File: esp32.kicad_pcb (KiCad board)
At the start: 2 copper layers, 44 x 80 mm, 102 parts, among them J1 USB_C, J14 PWR_CONN, J15 SPI_0, J16 SPI_1, J3 A0, J4 A1, J5 A2, J6 D0, J7 D1, J8 USB_VOUT, Q10 AO3400A, Q11 AO3400A, Q12 AO3400A, Q3 AO3400A, Q4 AO3400A, Q5 AO3400A, Q6 AO3400A, Q7 AO3400A, Q8 AO3400A, Q9 AO3400A, SW1 SW_RST, SW2 SW_BOOT, U1 LMR36520ADDAR, U3 ESP32-S3-WROOM-1

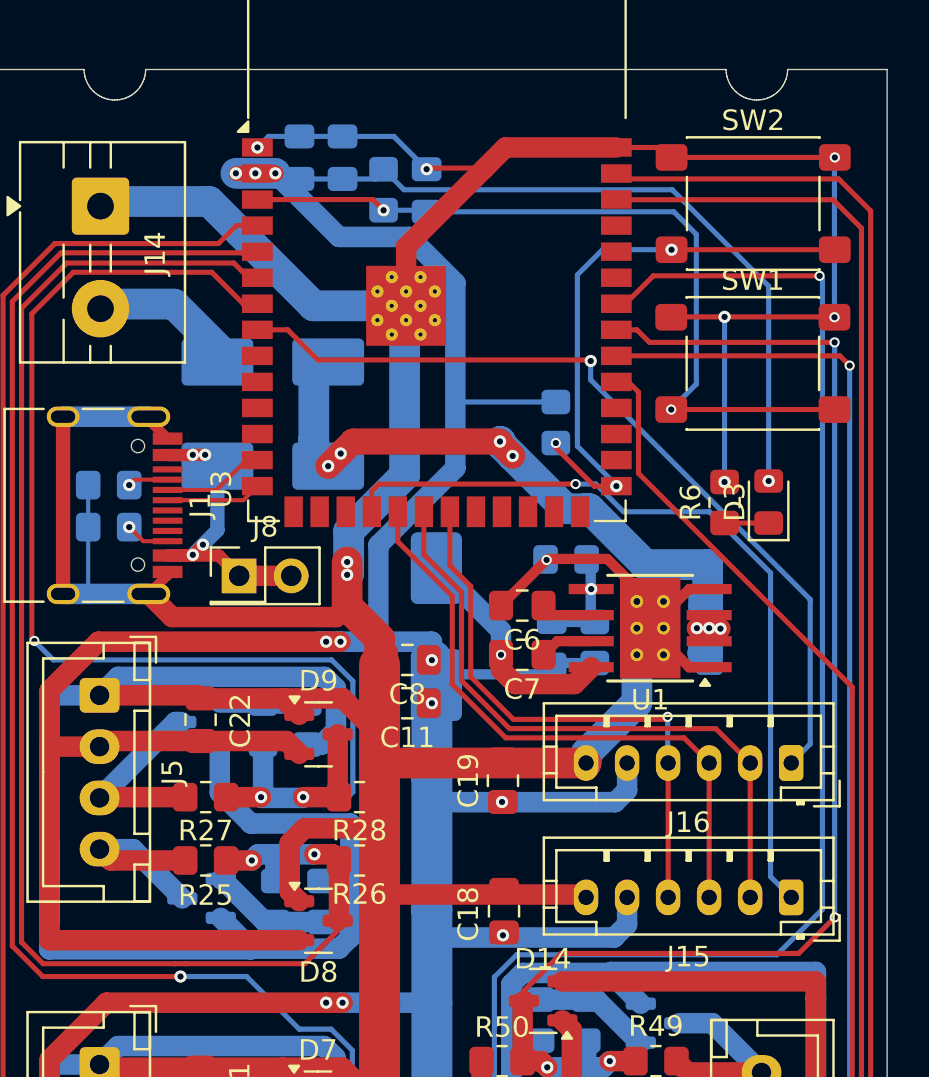
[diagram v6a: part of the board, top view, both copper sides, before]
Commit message: remove vias from pads
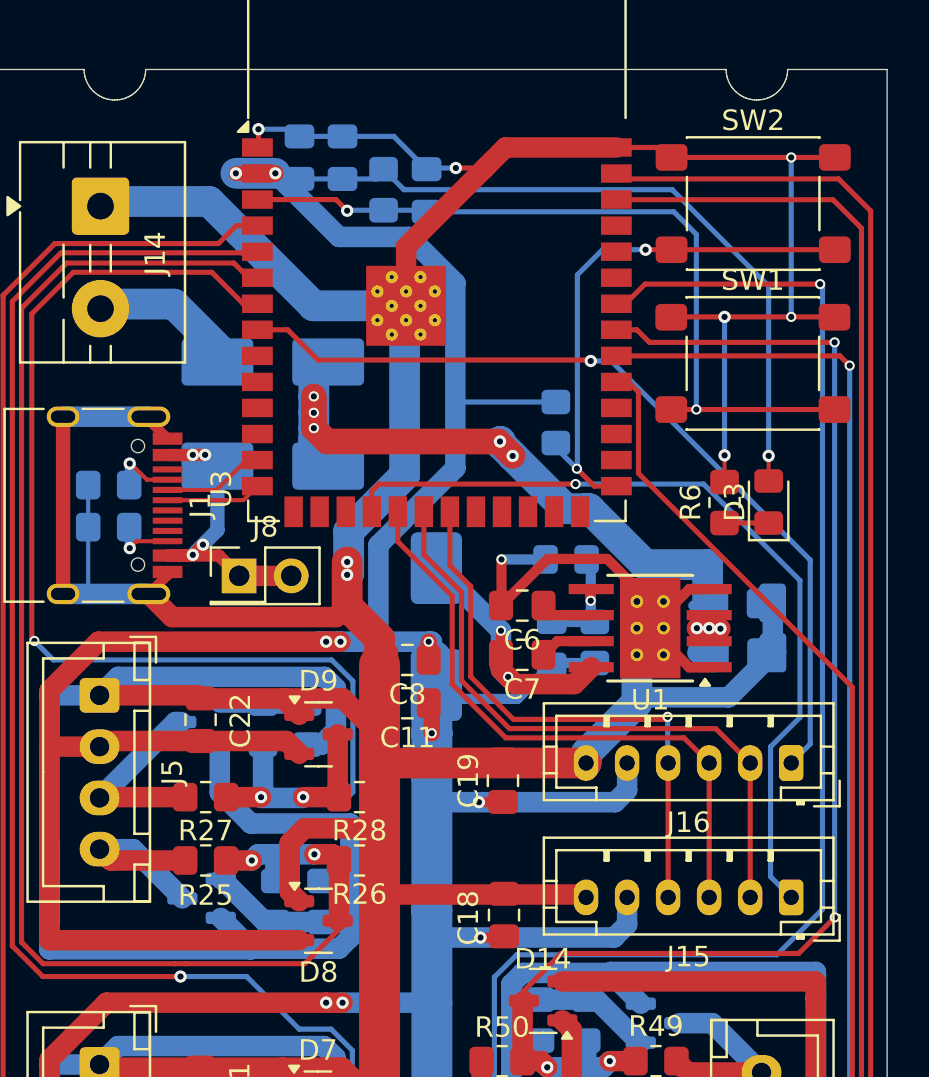
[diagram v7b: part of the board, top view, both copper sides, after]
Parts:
- moved C5 2.96 mm to (107.6, 99.4), turned to 0 degrees
- moved C4 2.93 mm to (107.6, 97.0), turned to 0 degrees
- moved C18 0.19 mm to (96.2, 112.2)
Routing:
- net GND: track 699.2 -> 714.5 mm
- net VCC: track 43.9 -> 38.7 mm, vias 7 -> 8
- net +3V3: track 443.8 -> 447.4 mm, vias 19 -> 18
- net Net-(U1-SW): track 11.3 -> 13.7 mm, vias 1 -> 2
- net /SPI_CS0: track 38.6 -> 40.4 mm
- net /GPIO0: track 27.9 -> 26.5 mm, vias 3 -> 2
- net Net-(J1-CC1): track 1.98 -> 3.23 mm
- net /EN: track 39.7 -> 38.6 mm
- net Net-(J1-CC2): track 2.16 -> 3.02 mm
- net Net-(U1-FB): track 5.02 -> 5.60 mm
- net /SPI_CS1: track 41.4 -> 42.0 mm
- net /D3: track 80.0 -> 79.5 mm

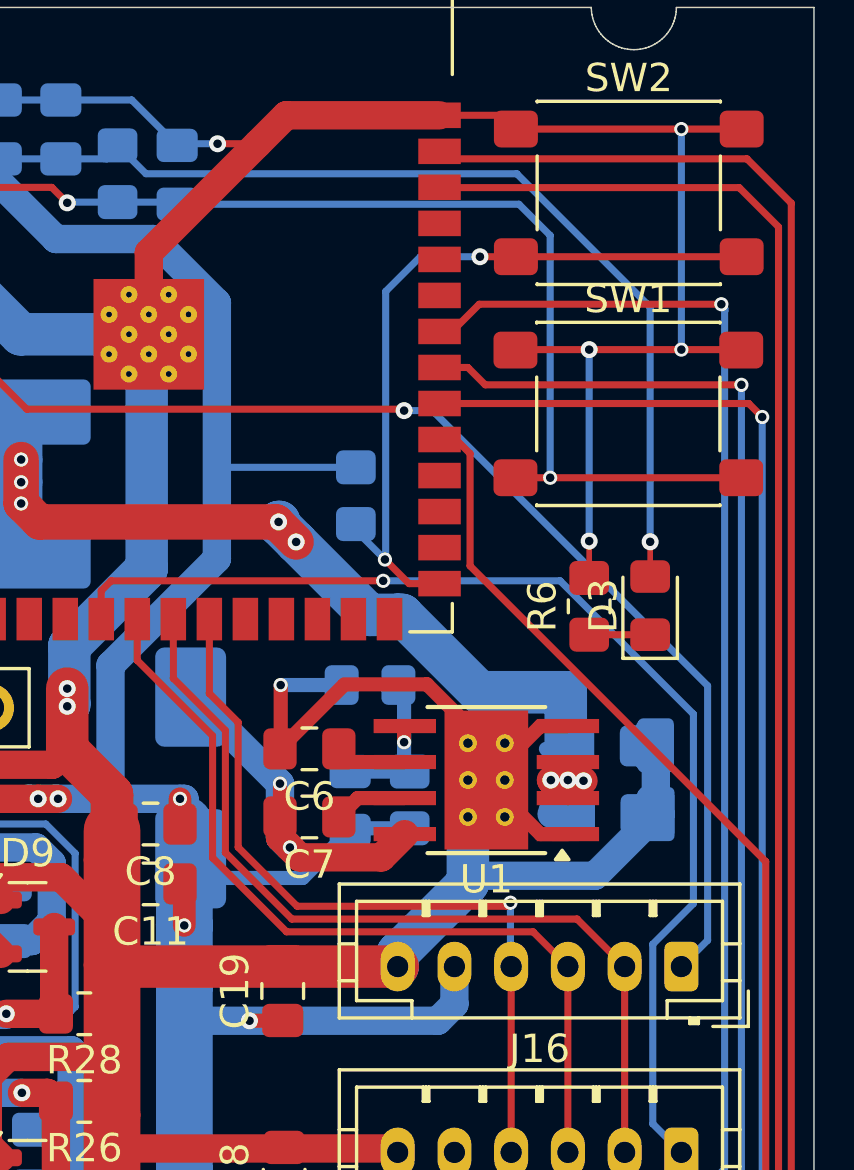
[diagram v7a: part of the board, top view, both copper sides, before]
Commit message: swap diode place
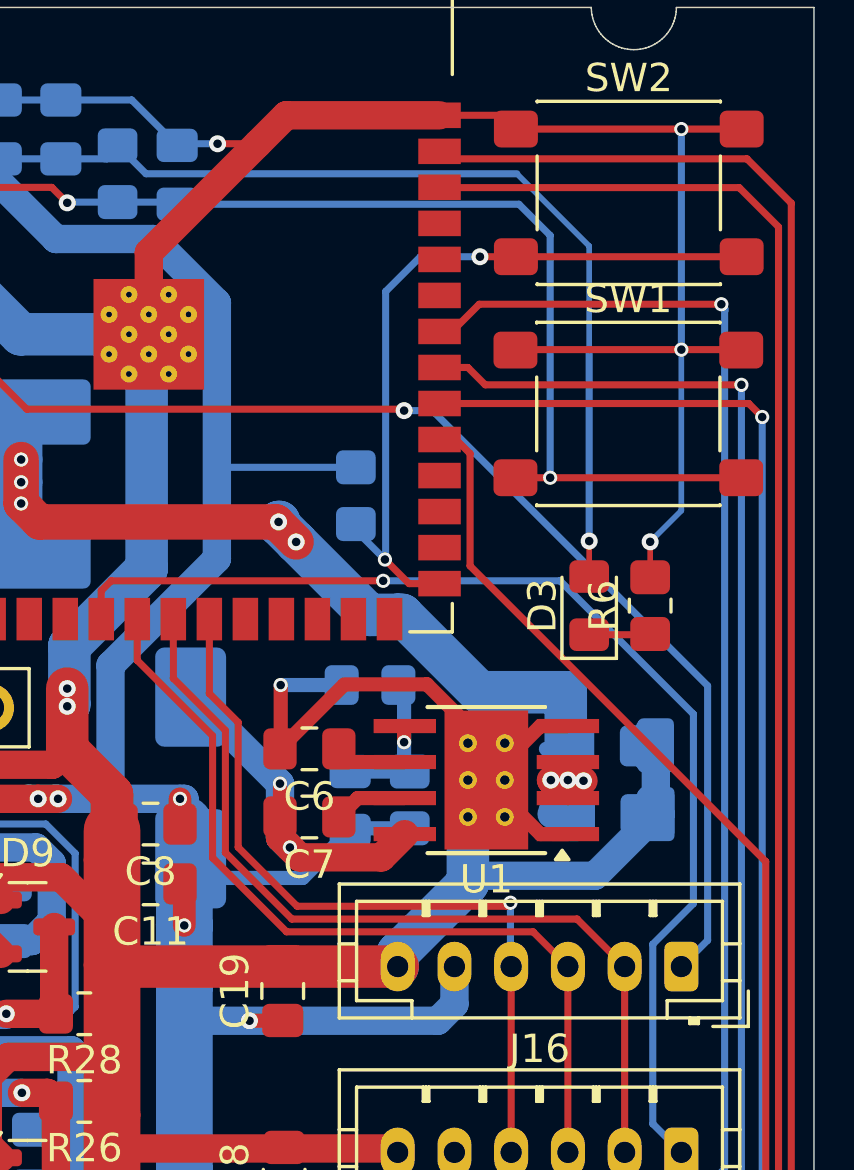
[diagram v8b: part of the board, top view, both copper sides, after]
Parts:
- moved R6 2.15 mm to (109.1, 92.0)
- moved D3 2.15 mm to (107.0, 92.0)
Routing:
- net +3V3: track 447.4 -> 446.4 mm
- net GND: track 714.5 -> 714.9 mm, vias 9 -> 8
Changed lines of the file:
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@@
 	(footprint "LED_SMD:LED_0805_2012Metric_Pad1.15x1.40mm_HandSolder"
 		(layer "F.Cu")
-		(at 109.1 92.05 90)
+		(at 106.95 92.05 90)
 		(descr "LED SMD 0805 (2012 Metric), square (rectangular) end terminal, IPC-7351 nominal, (Body size source: https://docs.google.com/spreadsheets/d/1BsfQQcO9C6DZCsRaXUlFlo91Tg2WpOkGARC1WS5S8t0/edit?usp=sharing), generated with kicad-footprint-generator")
 		(tags "LED handsolder")
@@
 	(footprint "Resistor_SMD:R_0805_2012Metric_Pad1.20x1.40mm_HandSolder"
 		(layer "F.Cu")
-		(at 106.95 92.075 90)
+		(at 109.1 92.05 90)
 		(descr "Resistor SMD 0805 (2012 Metric), square (rectangular) end terminal, IPC-7351 nominal with elongated pad for handsoldering. (Body size source: IPC-SM-782 page 72, https://www.pcb-3d.com/wordpress/wp-content/uploads/ipc-sm-782a_amendment_1_and_2.pdf), generated with kicad-footprint-generator")
 		(tags "resistor handsolder")
@@
 	)
 	(segment
+		(start 109.1 89.8)
+		(end 109.1 91.025)
+		(width 0.2)
+		(layer "F.Cu")
+		(net 1)
+	)
+	(segment
 		(start 101.675 74.765)
 		(end 96.269372 74.765)
@@
 	)
 	(segment
-		(start 106.95 89.775)
-		(end 106.95 91.075)
-		(width 0.2)
-		(layer "F.Cu")
-		(net 1)
-	)
-	(segment
 		(start 90.17953 104.775)
 		(end 90.12953 104.725)
@@
 	)
 	(via
-		(at 106.95 83.025)
+		(at 109.1 89.8)
 		(size 0.6)
 		(drill 0.3)
@@
 	)
 	(via
-		(at 106.95 89.775)
-		(size 0.6)
-		(drill 0.3)
-		(layers "F.Cu" "B.Cu")
-		(net 1)
-	)
-	(via
 		(at 110.2 83.025)
 		(size 0.5)
@@
 	)
 	(segment
-		(start 106.95 83.025)
-		(end 106.95 89.775)
-		(width 0.25)
+		(start 110.2 83.025)
+		(end 110.2 88.7)
+		(width 0.2)
 		(layer "B.Cu")
 		(net 1)
@@
 	)
 	(segment
+		(start 110.2 88.7)
+		(end 109.1 89.8)
+		(width 0.2)
+		(layer "B.Cu")
+		(net 1)
+	)
+	(segment
 		(start 111.404061 116.256704)
 		(end 111.402062 116.258703)
@@
 	)
 	(segment
-		(start 109.1 89.8)
-		(end 109.1 91.025)
-		(width 0.2)
-		(layer "F.Cu")
-		(net 2)
-	)
-	(segment
 		(start 76.818716 116.460702)
 		(end 74.04556 119.233858)
@@
 	)
 	(segment
+		(start 106.95 89.775)
+		(end 106.95 91.075)
+		(width 0.2)
+		(layer "F.Cu")
+		(net 2)
+	)
+	(segment
 		(start 76.418716 98.860702)
 		(end 87.525 98.860702)
@@
 	)
 	(via
-		(at 109.1 89.8)
+		(at 87.525 98.860702)
 		(size 0.6)
 		(drill 0.3)
@@
 	)
 	(via
-		(at 87.525 98.860702)
+		(at 95.05 113.284674)
 		(size 0.6)
 		(drill 0.3)
@@
 	)
 	(via
-		(at 95.05 113.284674)
+		(at 85.05 76.025)
 		(size 0.6)
 		(drill 0.3)
@@
 	)
 	(via
-		(at 85.05 76.025)
+		(at 88.226 98.860702)
 		(size 0.6)
 		(drill 0.3)
@@
 	)
 	(via
-		(at 88.226 98.860702)
+		(at 106.95 89.775)
 		(size 0.6)
 		(drill 0.3)
@@
 	)
 	(segment
+		(start 106.95 83.025)
+		(end 106.95 79.375)
+		(width 0.2)
+		(layer "B.Cu")
+		(net 2)
+	)
+	(segment
 		(start 86.225 76.3)
 		(end 88.325 76.3)
@@
 	)
 	(segment
-		(start 109.1 81.525)
-		(end 104.4 76.825)
+		(start 106.95 83.025)
+		(end 106.95 89.775)
 		(width 0.25)
 		(layer "B.Cu")
@@
 	)
 	(segment
+		(start 106.95 79.375)
+		(end 104.4 76.825)
+		(width 0.2)
+		(layer "B.Cu")
+		(net 2)
+	)
+	(segment
 		(start 88.226 98.860702)
 		(end 87.185702 98.860702)
@@
 	)
 	(segment
-		(start 109.1 89.8)
-		(end 109.1 81.525)
-		(width 0.25)
-		(layer "B.Cu")
-		(net 2)
-	)
-	(segment
 		(start 98.725 87.175)
 		(end 93.826 87.175)
@@
 		(width 1)
 		(layer "B.Cu")
-		(net 2)
-	)
-	(segment
-		(start 92.770152 105.370376)
-		(end 92.679826 105.460702)
-		(width 1)
-		(layer "B.Cu")
